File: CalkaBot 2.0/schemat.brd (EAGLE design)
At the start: 76.8 x 68.7 mm, 53 parts, among them IC1 TB6612FNG, IC2 LM339D, IC3 7806DT, Q1 16MHz, X1 MINI-USB_4P-85-32004-40X

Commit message: zapomiałem o ziemi
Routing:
- net GND: track 477.5 -> 534.1 mm, vias 6 -> 7
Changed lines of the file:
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@@
 <wire x1="9.9" y1="11.5" x2="5.2" y2="6.8" width="0.4" layer="16"/>
 <wire x1="67.1" y1="52" x2="72.7" y2="52" width="0.4" layer="16"/>
-<wire x1="78.3" y1="57.6" x2="78.3" y2="66" width="0.4" layer="16"/>
+<wire x1="78.3" y1="57.6" x2="78.3" y2="59.7" width="0.4" layer="16"/>
 <via x="78.3" y="66" extent="1-16" drill="1" diameter="1.3"/>
+<wire x1="78.3" y1="59.7" x2="78.3" y2="66" width="0.4" layer="16"/>
 <wire x1="72.7" y1="52" x2="78.3" y2="57.6" width="0.4" layer="16"/>
 <via x="5.2" y="66" extent="1-16" drill="1" diameter="1.3"/>
@@
 <wire x1="65.3" y1="18.35" x2="68.84" y2="14.81" width="0.4" layer="1"/>
 <wire x1="68.84" y1="14.81" x2="68.84" y2="10.67" width="0.4" layer="1"/>
+<wire x1="78.3" y1="57.6" x2="78.3" y2="1" width="0.4" layer="16"/>
+<via x="78.3" y="1" extent="1-16" drill="1" diameter="1.3"/>
 </signal>
 <signal name="RST">

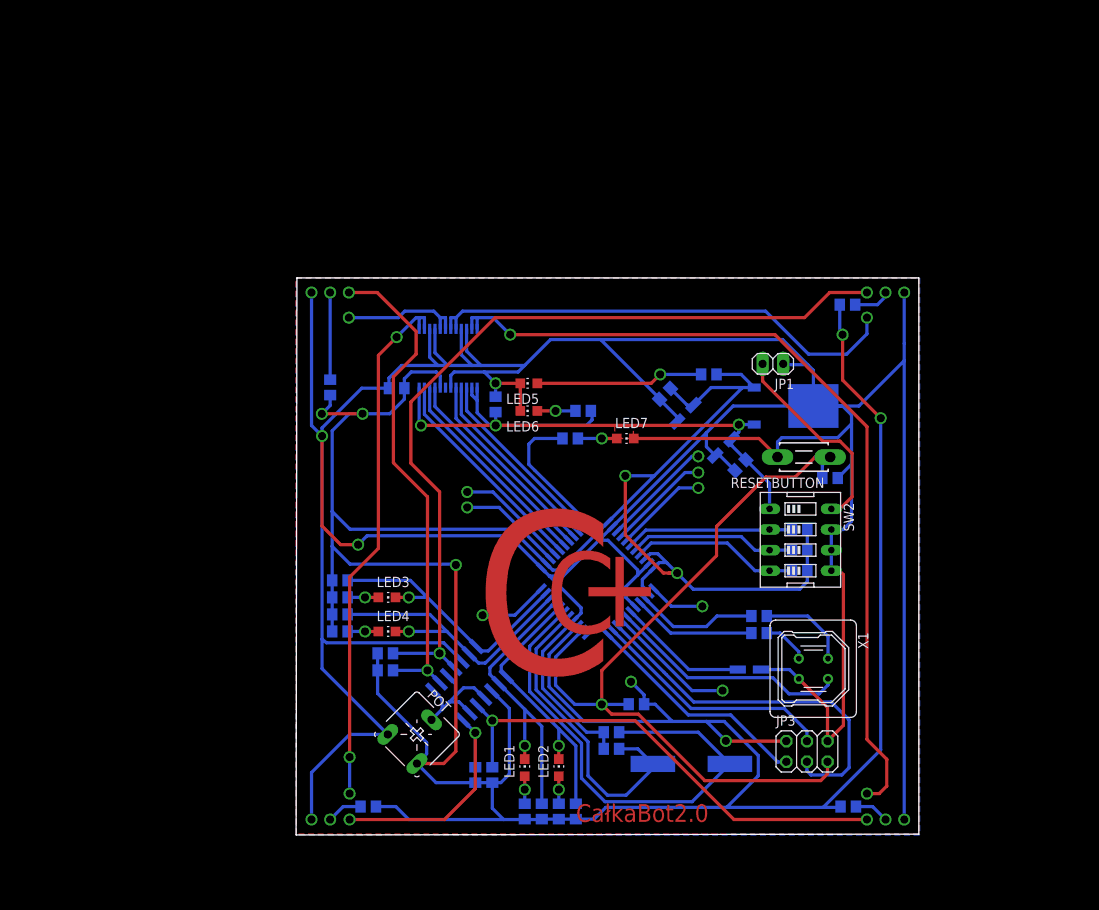
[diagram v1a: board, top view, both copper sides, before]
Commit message: Cały robot z kołami, redukcja miejsca
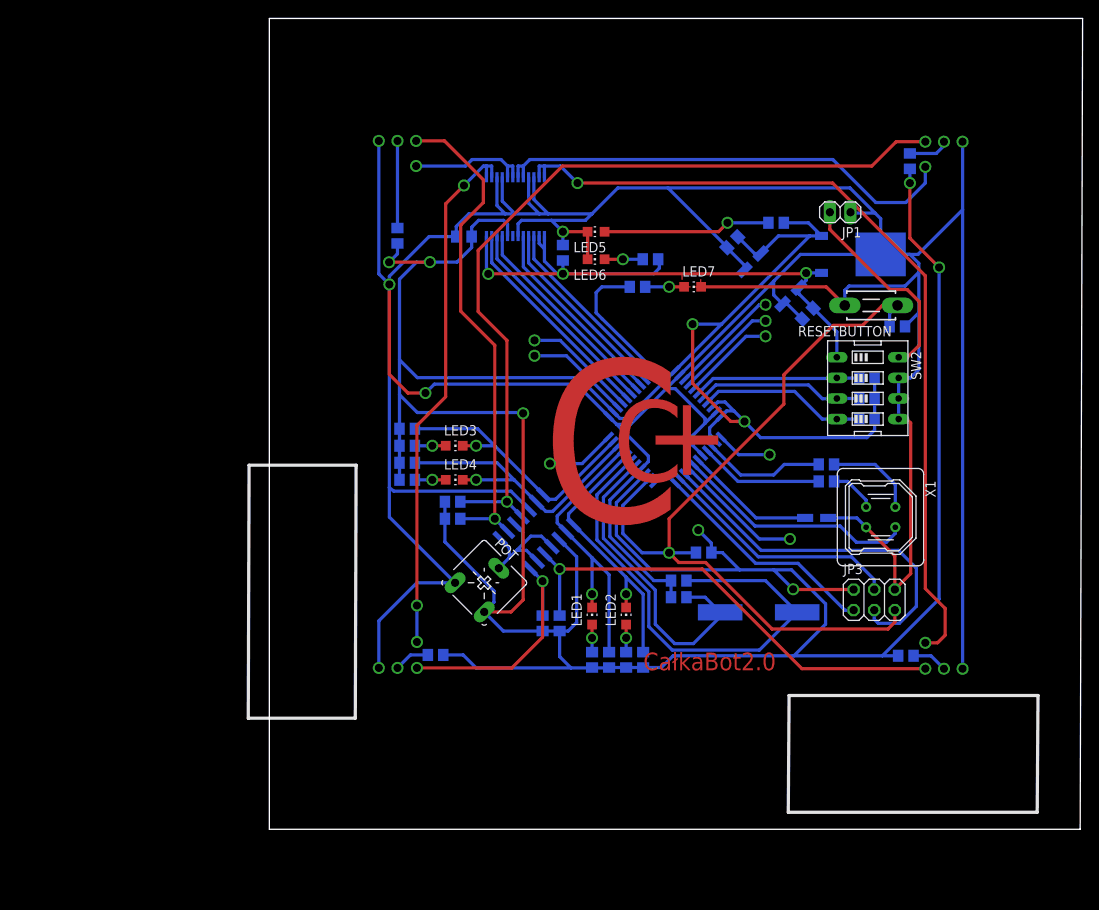
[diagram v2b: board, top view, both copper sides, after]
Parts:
- moved IC3 20.5 mm to (72.9, 70.7)
- moved C2 20.5 mm to (50.5, 28.4)
- moved C4 20.5 mm to (57.1, 72.2)
- moved C7 20.5 mm to (36.2, 70.9)
- moved C9 20.5 mm to (24.0, 72.9)
- moved IC1 20.5 mm to (30.4, 76.6)
- moved JP1 20.5 mm to (70.4, 75.9)
- moved LED3 20.5 mm to (22.8, 47.1)
- moved LED7 20.5 mm to (52.2, 66.7)
- moved Q1 20.5 mm to (60.4, 26.6)
- moved R10 20.5 mm to (22.6, 38.1)
- moved R13 20.5 mm to (22.6, 40.2)
- moved R16 20.5 mm to (17.0, 49.2)
- moved R20 20.5 mm to (17.0, 47.1)
- moved R25 20.5 mm to (68.7, 42.7)
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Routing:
- net VCC: track 468.6 -> 464.7 mm
- net BO2: track 59.7 -> 58.5 mm
- net S4: track 102.7 -> 101.6 mm
- net GND: track 534.1 -> 532.9 mm
- net BO1: track 105.2 -> 104.2 mm
- net S1: track 59.6 -> 58.6 mm
- net SCK: track 46.3 -> 45.5 mm
- removed copper zone on layer 16, net N$3
- removed copper zone on layer 16, net N$40
- removed copper zone on layer 1, net N$5
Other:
- board size 76.8 x 68.7 mm -> 100.3 x 100 mm

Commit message: redukcja miejsca, przygotowywanie pod dodawnie transoptora smd
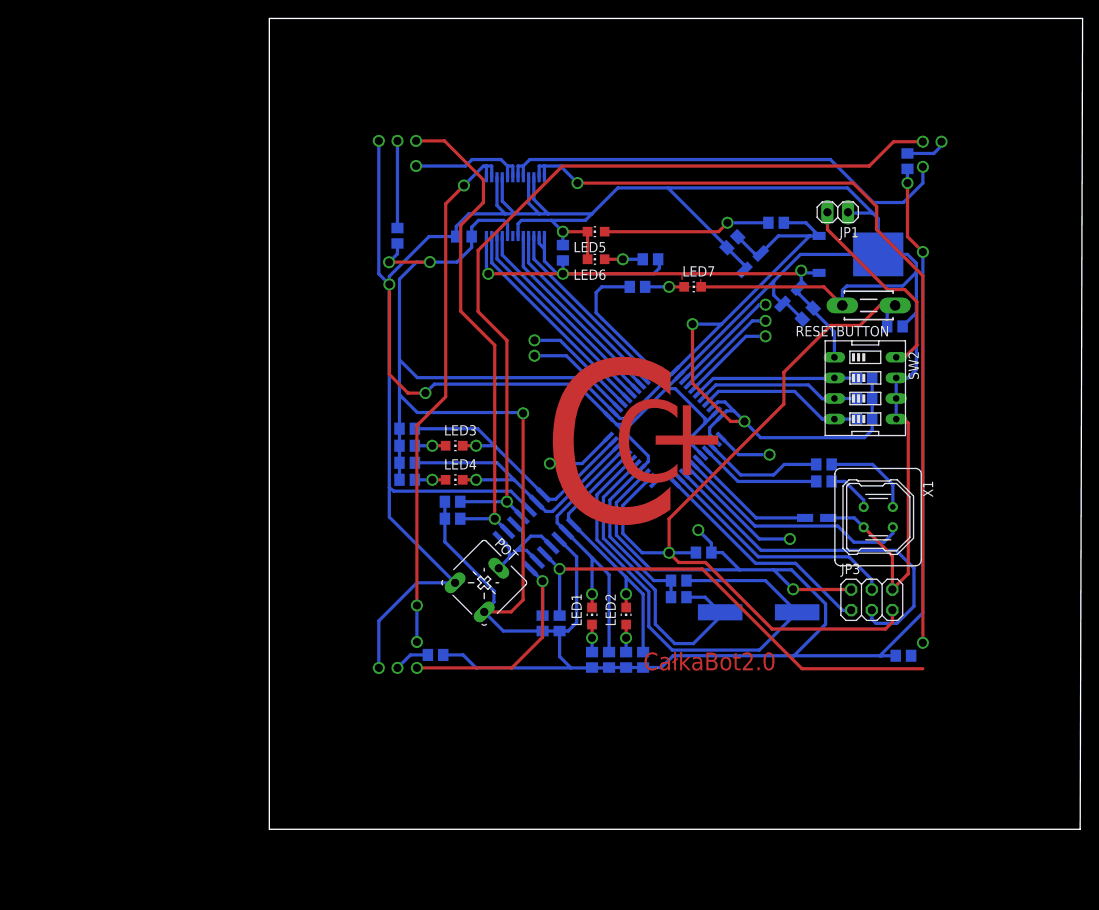
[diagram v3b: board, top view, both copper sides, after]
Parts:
- moved IC3 0.30 mm to (72.6, 70.7)
- moved JP1 0.30 mm to (70.1, 75.9)
- moved X1 0.30 mm to (75.1, 38.3)
- moved C3 0.30 mm to (77.2, 61.8)
- moved JP3 0.30 mm to (74.3, 28.1)
- moved R11 0.30 mm to (78.2, 21.2)
- moved R2 0.30 mm to (73.4, 50.4)
- moved R25 0.30 mm to (68.4, 42.7)
- moved R26 0.30 mm to (68.4, 44.8)
- moved R4 0.30 mm to (78.7, 82.2)
- moved R6 0.30 mm to (73.4, 52.9)
- moved R9 0.30 mm to (73.4, 55.5)
- moved RESETBUTTON 0.30 mm to (73.9, 64.4)
- moved SW2 0.30 mm to (73.5, 54.2)
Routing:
- net GND: track 532.9 -> 454.4 mm, vias 7 -> 5
- net N$23: track 4.41 -> 0.00 mm, vias 1 -> 0
- net VCC: track 464.7 -> 462.1 mm
- net BO1: track 104.2 -> 102.9 mm
- net S1: track 58.6 -> 58.3 mm, vias 2 -> 1

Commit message: dodałem koła i poczne ściany
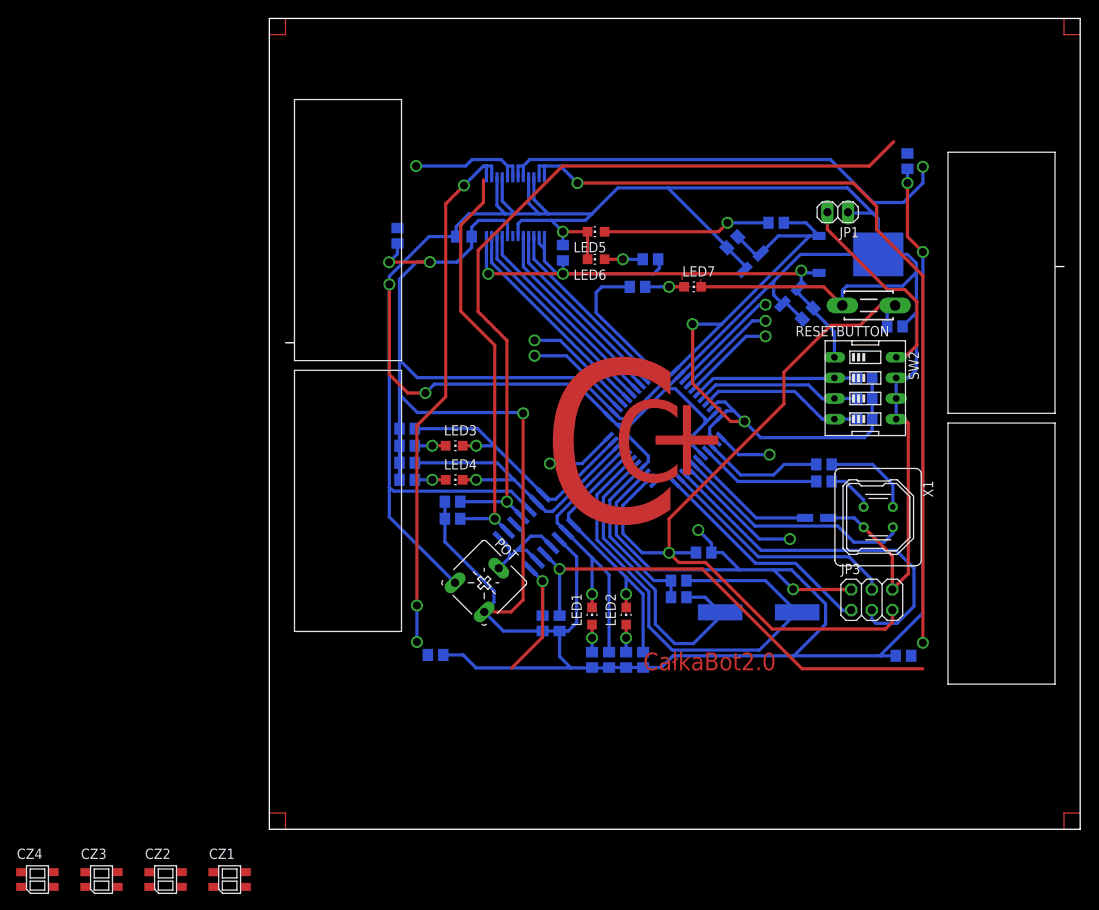
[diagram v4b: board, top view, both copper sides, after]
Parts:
- added CZ1, CZ2, CZ3, CZ4: KTIR0711S, ktir0711s:TOP
- added U$2, U$3, U$4, U$5: (no value), wheel:WHEEL
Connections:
- net GND: now also CZ1.EMITER, CZ1.KATODA, CZ2.EMITER, CZ2.KATODA, CZ3.EMITER, CZ3.KATODA, CZ4.EMITER, CZ4.KATODA
- net N$1: now also CZ1.ANODA
- net N$19: now also CZ2.ANODA
- net N$23: now also CZ3.ANODA
- net N$27: now also CZ4.ANODA
- net S1: now also CZ1.KOLEKTOR
- net S2: now also CZ2.KOLEKTOR
- net S3: now also CZ3.KOLEKTOR
- net S4: now also CZ4.KOLEKTOR
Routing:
- net GND: track 454.4 -> 419.0 mm, vias 5 -> 3
- net S2: track 30.4 -> 18.7 mm, vias 2 -> 1
- net N$19: track 10.8 -> 0.00 mm, vias 1 -> 0
- net S3: track 61.4 -> 51.2 mm, vias 2 -> 1
- net N$1: track 5.09 -> 0.00 mm, vias 1 -> 0
- net N$27: track 4.41 -> 0.00 mm, vias 1 -> 0
- net N$8: track 0.00 -> 4.00 mm
- net N$6: track 0.00 -> 4.00 mm
- net N$5: track 0.00 -> 4.00 mm
- net N$3: track 0.00 -> 4.00 mm
- net S4: track 101.3 -> 97.7 mm, vias 2 -> 1
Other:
- board size 100.3 x 100 mm -> 100 x 100 mm

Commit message: nie starcza mi miejsca nie wiem o co cmon
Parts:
- moved CZ3 139.8 mm to (90.4, 78.4), flipped to the bottom, turned to 180 degrees
- moved CZ4 119.6 mm to (90.4, 5.30), flipped to the bottom
- moved CZ1 86.3 mm to (11.0, 78.4), flipped to the bottom, turned to 180 degrees
- moved R8 61.4 mm to (28.6, 13.0), turned to 180 degrees
- moved R14 59.9 mm to (80.3, 17.7), turned to 90 degrees
- moved R4 59.6 mm to (19.4, 75.9), turned to 180 degrees
- moved R11 54.2 mm to (80.4, 75.4), turned to 270 degrees
- moved C9 51.9 mm to (28.7, 21.2), turned to 90 degrees
- moved R21 50.6 mm to (58.7, 14.2), turned to 270 degrees
- moved R17 50.2 mm to (56.6, 14.2), turned to 270 degrees
- moved R20 49.9 mm to (54.5, 14.2), turned to 270 degrees
- moved R16 49.8 mm to (52.4, 14.2), turned to 270 degrees
- moved IC1 49.3 mm to (25.0, 27.6), turned to 90 degrees
- moved POT 45.4 mm to (71.4, 23.7), turned to 45 degrees
- moved JP1 45.2 mm to (25.7, 67.3), turned to 270 degrees
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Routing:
- net AO2: track 15.4 -> 9.26 mm, vias 1 -> 0
- net S4: track 97.7 -> 93.4 mm
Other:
- outline, holes or cut-outs redrawn

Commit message: Mogę już podłączyć na transoptory
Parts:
- moved CZ3 6.24 mm to (88.1, 84.2)
- moved CZ1 6.24 mm to (8.70, 84.2)
- moved R11 2.86 mm to (78.1, 73.7)
- moved R18 2.86 mm to (78.6, 35.3)
- moved R19 2.86 mm to (78.6, 39.5)
- moved R5 2.86 mm to (78.6, 37.4)
- moved CZ4 2.86 mm to (88.1, 3.60)
- moved POT 2.86 mm to (69.1, 22.0)
- moved R3 2.86 mm to (74.1, 31.3)
- moved R7 2.86 mm to (74.1, 29.2)
- moved C2 2.86 mm to (70.9, 46.0)
- moved R15 2.86 mm to (78.6, 41.6)
- moved C5 2.86 mm to (35.9, 61.9)
- moved LED4 2.86 mm to (56.4, 18.3)
- moved R17 2.86 mm to (54.3, 12.5)
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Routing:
- net S1: track 58.3 -> 8.38 mm
- net S4: track 93.4 -> 46.1 mm, vias 1 -> 2
- net S3: track 51.2 -> 8.66 mm
- net N$27: track 0.00 -> 24.0 mm
- net S2: track 18.7 -> 6.46 mm
- net GND: track 419.0 -> 423.7 mm
- net AO1: track 65.9 -> 61.4 mm, vias 3 -> 1
- net VCC: track 462.1 -> 459.0 mm
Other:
- outline, holes or cut-outs redrawn

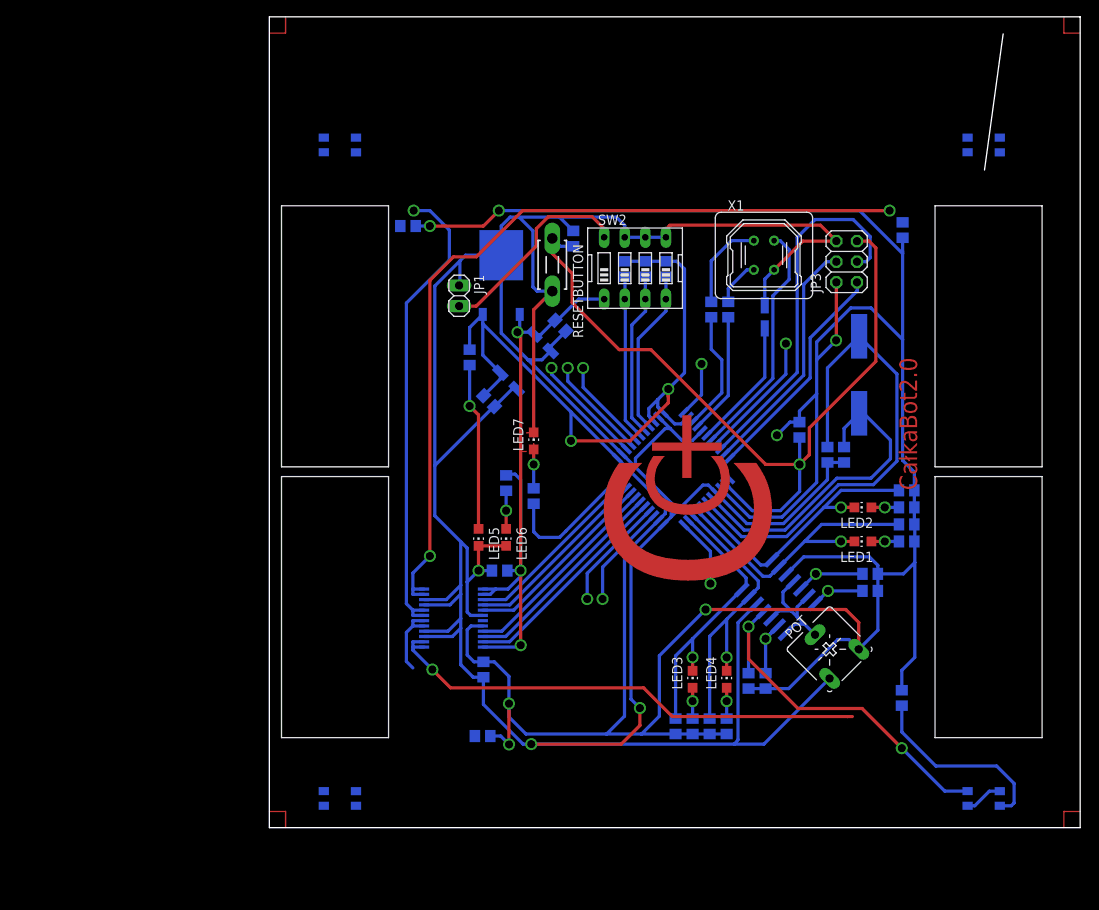
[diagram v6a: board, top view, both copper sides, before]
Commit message: Podłączone transoptory, trzeba rozkminić jak podłączyć gniazda
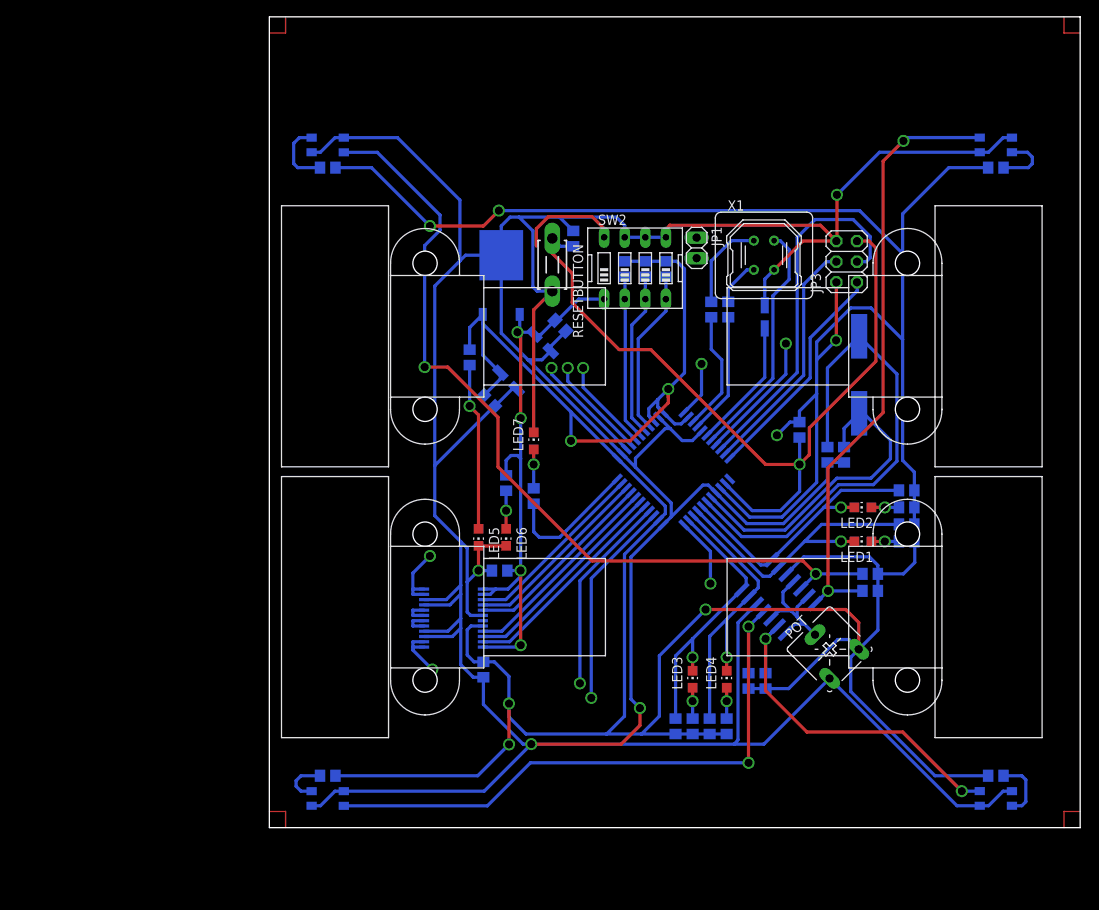
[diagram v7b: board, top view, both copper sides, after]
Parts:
- added U$6, U$7, U$8, U$9: (no value), PololuMG_v2:HP_NM
- moved CZ1 114.2 mm to (89.6, 3.60), turned to 0 degrees
- moved CZ2 114.2 mm to (89.6, 84.2)
- moved R8 94.5 mm to (89.6, 81.4), turned to 0 degrees
- moved CZ3 80.9 mm to (7.20, 84.2)
- moved CZ4 80.9 mm to (7.20, 3.60), turned to 180 degrees
- moved R14 71.4 mm to (7.20, 6.40), turned to 180 degrees
- moved R11 68.3 mm to (89.6, 6.40), turned to 0 degrees
- moved JP1 29.9 mm to (52.7, 71.5)
- moved R4 12.2 mm to (7.20, 81.4)
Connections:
- removed net S1: CZ1.KOLEKTOR, IC2.5, R3.1
- new net N$14: CZ3.ANODA, R4.1
- net N$1: now also CZ3.KOLEKTOR, IC2.5, R3.1; no longer CZ1.ANODA, R4.1
- net N$23: now also CZ1.ANODA; no longer CZ3.ANODA
- net S3: now also CZ1.KOLEKTOR; no longer CZ3.KOLEKTOR
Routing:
- net GND: track 423.7 -> 535.8 mm, vias 3 -> 4
- net N$1: track 0.00 -> 105.4 mm, vias 0 -> 2
- net BO1: track 102.9 -> 8.36 mm, vias 2 -> 1
- net S2: track 6.46 -> 75.4 mm, vias 1 -> 2
- net VCC: track 459.0 -> 518.2 mm
- net BO2: track 58.2 -> 3.42 mm, vias 1 -> 0
- net AO1: track 61.4 -> 7.19 mm
- net S3: track 8.66 -> 46.6 mm, vias 1 -> 2
- net S4: track 46.1 -> 77.3 mm
- net N$27: track 24.0 -> 6.06 mm
- net I/O9: track 12.9 -> 25.7 mm
- net PIN: track 25.4 -> 12.8 mm
- net I/O7: track 14.0 -> 24.8 mm
- net VM: track 81.4 -> 72.6 mm, vias 3 -> 4
- net N$14: track 0.00 -> 8.46 mm
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- removed copper zone on layer 1, net N$42
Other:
- outline, holes or cut-outs redrawn
- board text removed: "+"
- board text removed: "C"
- board text removed: "CałkaBot2.0"
